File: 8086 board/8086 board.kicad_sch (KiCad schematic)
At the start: 9 parts, among them U1 P8086-2, U23 74HC14, U27 74HC02, U8 74AC00

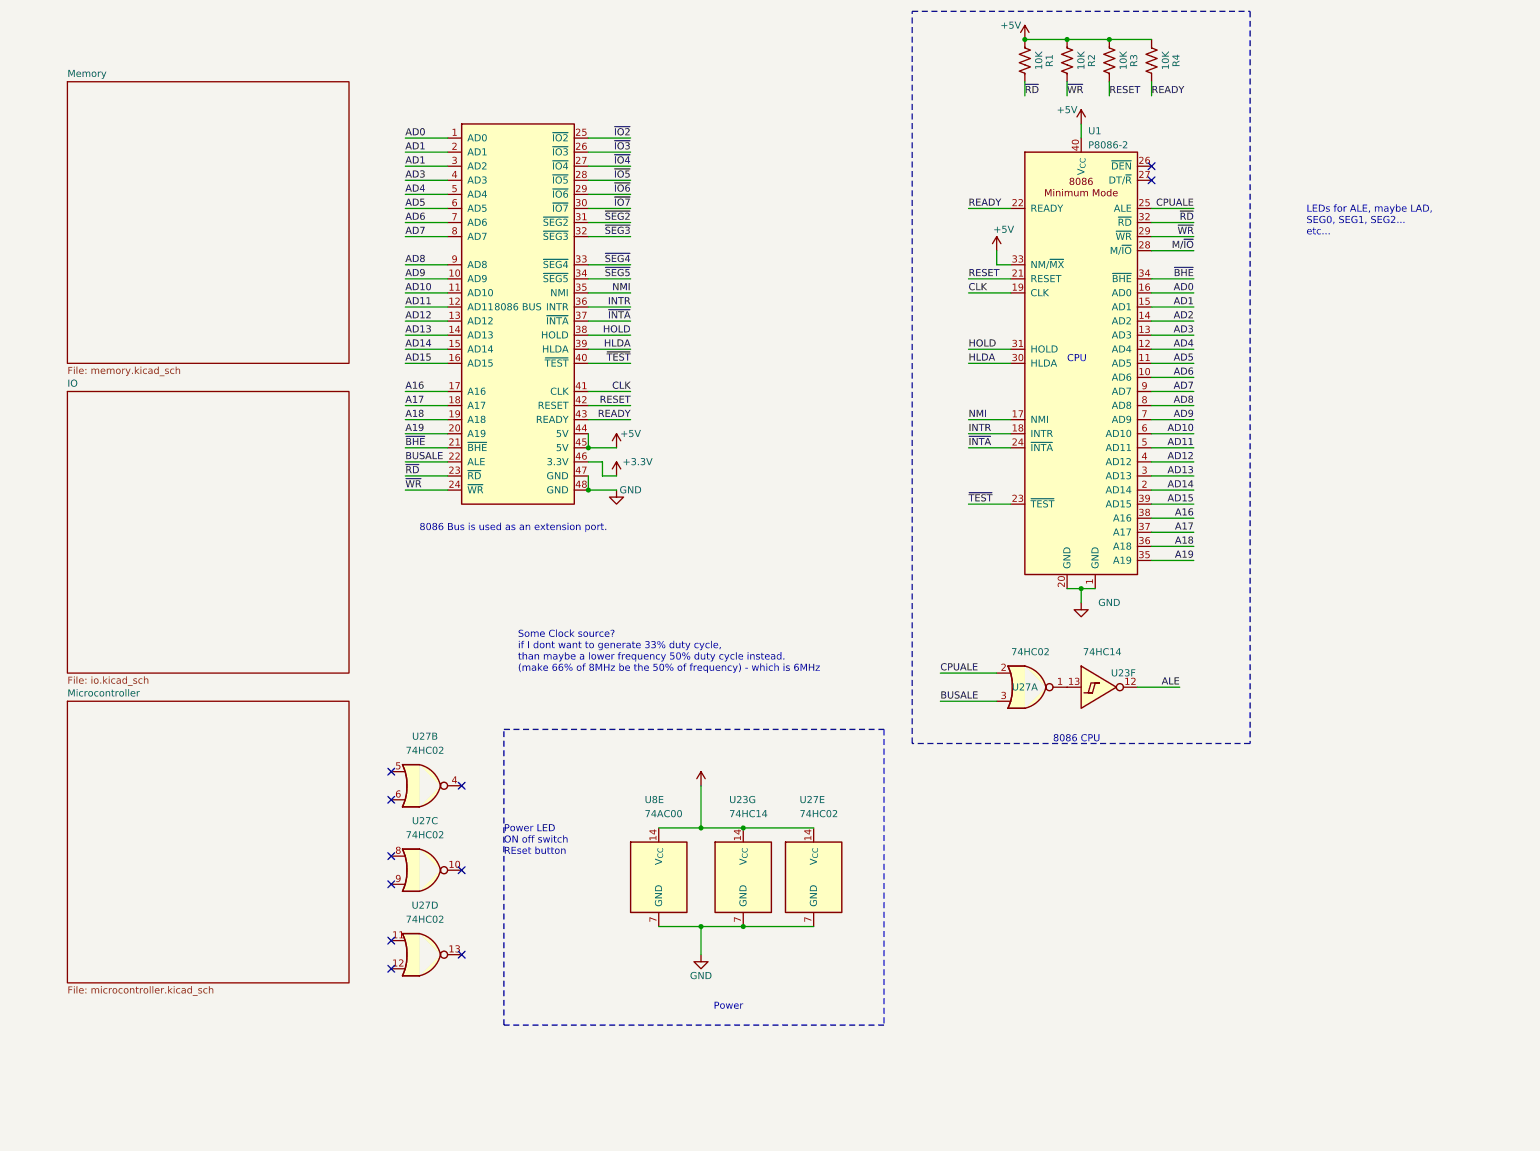
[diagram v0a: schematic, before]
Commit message: better schematic. initial pcb layout
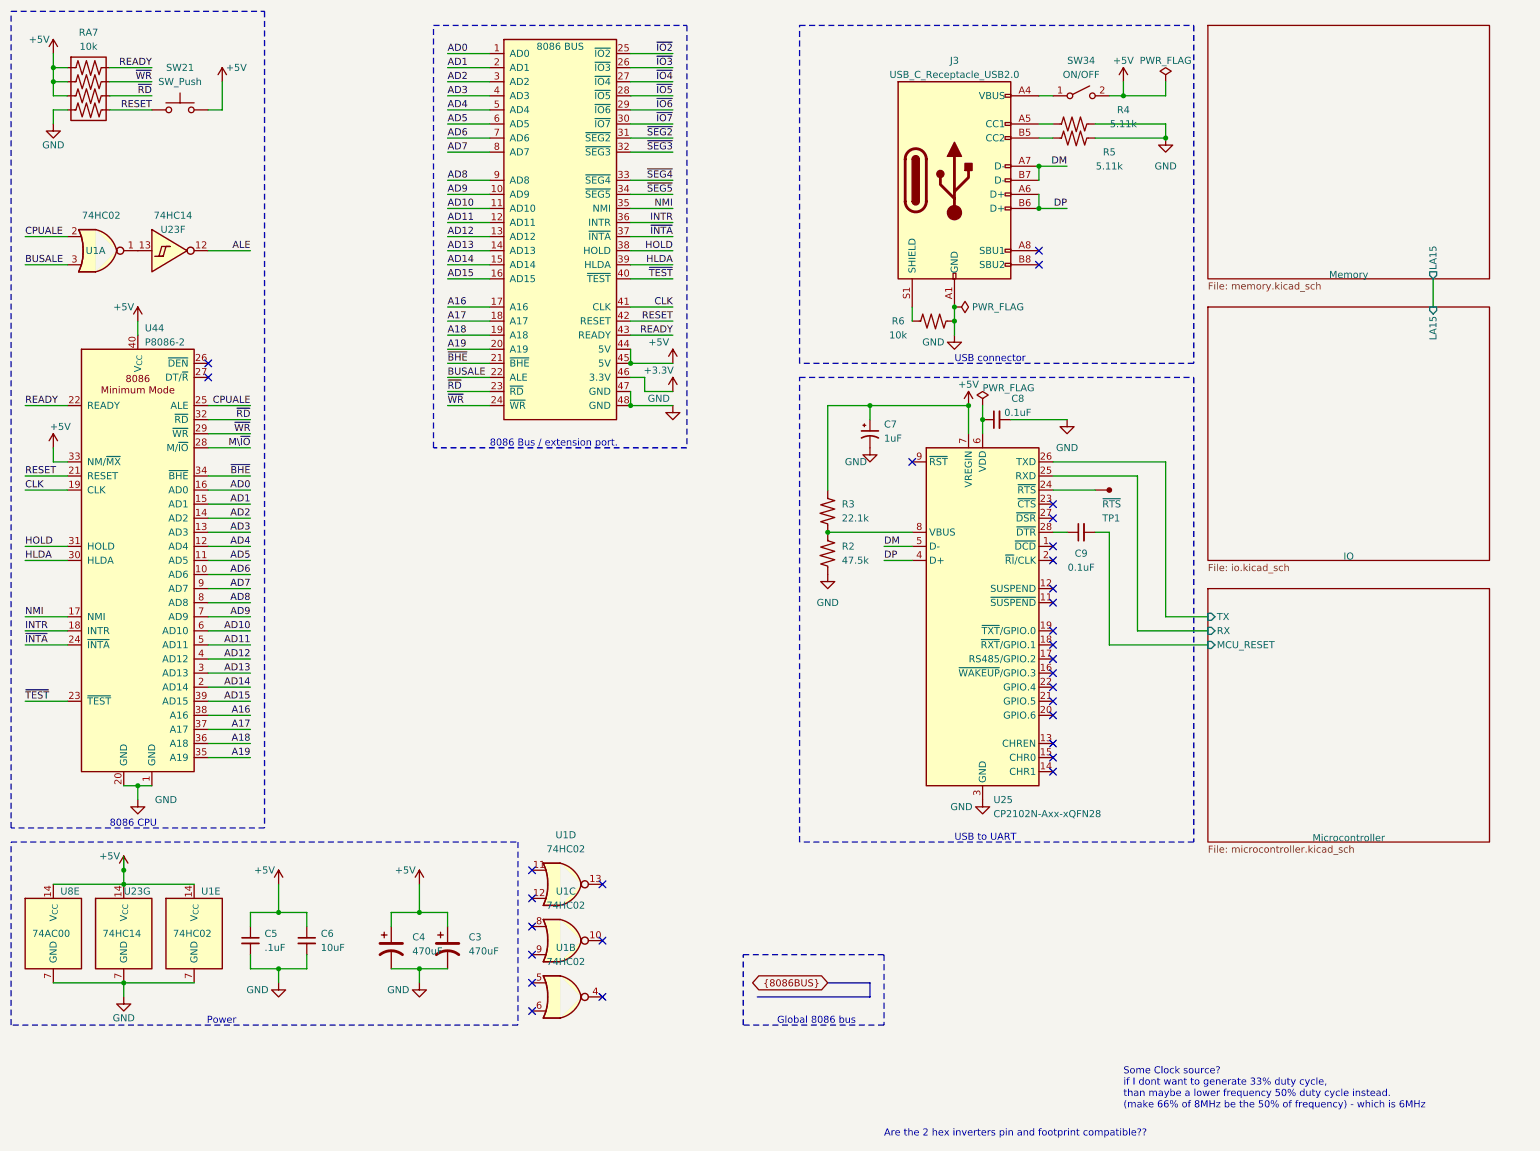
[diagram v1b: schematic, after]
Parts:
- removed R1, R2, R3, R4: 10K, Resistor_SMD:R_0603_1608Metric_Pad0.98x0.95mm_HandSolder, symbol Device:R_US
- added C3, C4: 470uF, symbol Device:C_Polarized_US
- added C5: .1uF, symbol Device:C_Small
- added C6: 10uF, symbol Device:C_Small
- added C7: 1uF, symbol Device:C_Polarized_Small_US
- added C8, C9: 0.1uF, symbol Device:C_Small
- added J3: USB_C_Receptacle_USB2.0, symbol Connector:USB_C_Receptacle_USB2.0
- added R2: 47.5k, symbol 8086PC:R
- added R3: 22.1k, symbol 8086PC:R
- added R4, R5: 5.11k, symbol 8086PC:R
- added R6: 10k, symbol 8086PC:R
- added RA7: 10k, Resistor_SMD:R_Array_Concave_4x0603, symbol 8086PC:R_Array_4
- added SW21: SW_Push, Button_Switch_SMD:SW_Push_1P1T_NO_6x6mm_H9.5mm, symbol Switch:SW_Push
- added SW34: ON/OFF, symbol Switch:SW_SPST
- added TP1: ~{RTS}, symbol 8086PC:TestPoint
- added U25: CP2102N-Axx-xQFN28, Package_DFN_QFN:QFN-28-1EP_5x5mm_P0.5mm_EP3.35x3.35mm, symbol Interface_USB:CP2102N-Axx-xQFN28
- renumbered U27 to U1, U1 to U44
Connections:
- net +5V: now also C3.1, C4.1, C5.1, C6.1, C7.1, R3.1, RA7.1, RA7.2, RA7.3, SW21.1, SW34.2 (B), U25.7 (VREGIN)
- net AD1: no longer BUS1.3 (AD2)
- net AD2: now also BUS1.3 (AD2)
- net GND: now also C3.2, C4.2, C5.2, C6.2, C7.2, C8.2, J3.A1 (GND), J3.A12 (GND), J3.B1 (GND), J3.B12 (GND), R2.2, R4.2, R5.2, R6.2, RA7.4, U25.29 (GND), U25.3 (GND)
- net READY: now also RA7.8
- net RESET: now also RA7.5, SW21.2
- net ~{RD}: now also RA7.6
- net ~{WR}: now also RA7.7
- net M/~{IO} renamed M\~{IO}
- new net: J3.B5 (CC2), R5.1
- new net: TP1.1, U25.24 (~{RTS})
- new net: C9.1, U25.28 (~{DTR})
- new net: C8.1, U25.6 (VDD)
- new net: R2.1, R3.2, U25.8 (VBUS)
- new net: J3.A4 (VBUS), J3.A9 (VBUS), J3.B4 (VBUS), J3.B9 (VBUS), SW34.1 (A)
- new net: J3.S1 (SHIELD), R6.1
- new net: J3.A5 (CC1), R4.1
- new net DM: J3.A7 (D-), J3.B7 (D-), U25.5 (D-)
- new net DP: J3.A6 (D+), J3.B6 (D+), U25.4 (D+)
- new net Microcontroller/MCU_RESET: C9.2
- new net Microcontroller/RX: U25.25 (RXD)
- new net Microcontroller/TX: U25.26 (TXD)
- no-connect marks 11 -> 30
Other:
- sheet IO ports: added LA15; removed none
- sheet Memory ports: added LA15; removed none
- sheet Microcontroller ports: added MCU_RESET, RX, TX; removed none
- note added: "8086 Bus / extension port."
- note added: "Are the 2 hex inverters pin and footprint compatible??"
- note added: "Global 8086 bus"
- note added: "USB connector"
- note added: "USB to UART"
- note removed: "8086 Bus is used as an extension port."
- note removed: "CPU"
- note removed: "LEDs for ALE, maybe LAD, SEG0, SEG1, SEG2... etc..."
- note removed: "Power LED ON off switch REset button"
- moved on the sheet: U1A, U1B, U1C, U1D, U1E, U23F, U23G, U44, U8E

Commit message: Schematic finished! (some footprint assignments are still needed)
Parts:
- removed C3: 470uF, symbol Device:C_Polarized_US
- removed C5: .1uF, symbol Device:C_Small
- removed C6: 10uF, symbol Device:C_Small
- removed C7: 1uF, symbol Device:C_Polarized_Small_US
- removed unit 3 of U1
- removed unit 2 of U1
- added C? (x36): 1uF, Capacitor_SMD:C_0603_1608Metric_Pad1.08x0.95mm_HandSolder, symbol Device:C_Small
- added C? (x2): 10uF, Capacitor_SMD:C_0603_1608Metric_Pad1.08x0.95mm_HandSolder, symbol Device:C_Polarized_US
- added U?: 74HC02, Package_SO:SOIC-14_3.9x8.7mm_P1.27mm, symbol 8086PC:74HC02
- added U?: AMS1117-3.3, Package_TO_SOT_SMD:SOT-223-3_TabPin2, symbol Regulator_Linear:AMS1117-3.3
- BUS1: footprint Package_DIP:SMDIP-64_W15.24mm -> Connector_PinHeader_2.54mm:PinHeader_2x24_P2.54mm_Vertical
- C4: renamed from C8; value 0.1uF -> 1uF; footprint (none) -> Capacitor_SMD:C_0603_1608Metric_Pad1.08x0.95mm_HandSolder
- C5: renamed from C9; footprint (none) -> Capacitor_SMD:C_0603_1608Metric_Pad1.08x0.95mm_HandSolder
- R1: renamed from R4; footprint (none) -> Resistor_SMD:R_0603_1608Metric_Pad0.98x0.95mm_HandSolder
- R2: renamed from R5; footprint (none) -> Resistor_SMD:R_0603_1608Metric_Pad0.98x0.95mm_HandSolder
- R3: renamed from R6; footprint (none) -> Resistor_SMD:R_0603_1608Metric_Pad0.98x0.95mm_HandSolder
- R4: renamed from R3; footprint (none) -> Resistor_SMD:R_0603_1608Metric_Pad0.98x0.95mm_HandSolder
- R5: renamed from R2; footprint (none) -> Resistor_SMD:R_0603_1608Metric_Pad0.98x0.95mm_HandSolder
- SW34: value ON/OFF -> POWER
- SW?: renamed from SW21; value SW_Push -> RESET; footprint Button_Switch_SMD:SW_Push_1P1T_NO_6x6mm_H9.5mm -> 8086PC:SW_Push_1P1T_NO_6x6mm_H9.5mm; symbol Switch:SW_Push -> 8086PC:SW_Push
- TP1: footprint (none) -> TestPoint:TestPoint_Pad_1.5x1.5mm
- renumbered C4 to C?, J3 to J1, RA7 to RA1, U44 to U1, U8 to U2, U23 to U3, U1 to U4, U25 to U?
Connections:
- net +3.3V: now also BUS1.44 (3.3V), C?.1, U?.2 (VO); no longer BUS1.46 (3.3V)
- net +5V: now also BUS1.40 (5V), BUS1.42 (5V), C?.1, C?.1, C?.1, C?.1, C?.1, C?.1, C?.1, C?.1, C?.1, C?.1, C?.1, C?.1, C?.1, C?.1, C?.1, C?.1, C?.1, C?.1, C?.1, C?.1, C?.1, C?.1, C?.1, C?.1, C?.1, C?.1, C?.1, C?.1, C?.1, C?.1, C?.1, C?.1, C?.1, C?.1, C?.1, C?.1, C?.1, U?.14 (V_{CC}), U?.3 (VI); no longer BUS1.44 (5V), BUS1.45 (5V)
- net A16: now also BUS1.33 (A16); no longer BUS1.17 (A16)
- net A17: now also BUS1.35 (A17); no longer BUS1.18 (A17)
- net A18: now also BUS1.37 (A18); no longer BUS1.19 (A18)
- net A19: now also BUS1.39 (A19); no longer BUS1.20 (A19)
- net AD1: now also BUS1.3 (AD1); no longer BUS1.2 (AD1)
- net AD10: now also BUS1.21 (AD10); no longer BUS1.11 (AD10)
- net AD11: now also BUS1.23 (AD11); no longer BUS1.12 (AD11)
- net AD12: now also BUS1.25 (AD12); no longer BUS1.13 (AD12)
- net AD13: now also BUS1.27 (AD13); no longer BUS1.14 (AD13)
- net AD14: now also BUS1.29 (AD14); no longer BUS1.15 (AD14)
- net AD15: now also BUS1.31 (AD15); no longer BUS1.16 (AD15)
- net AD2: now also BUS1.5 (AD2); no longer BUS1.3 (AD2)
- net AD3: now also BUS1.7 (AD3); no longer BUS1.4 (AD3)
- net AD4: now also BUS1.9 (AD4); no longer BUS1.5 (AD4)
- net AD5: now also BUS1.11 (AD5); no longer BUS1.6 (AD5)
- net AD6: now also BUS1.13 (AD6); no longer BUS1.7 (AD6)
- net AD7: now also BUS1.15 (AD7); no longer BUS1.8 (AD7)
- net AD8: now also BUS1.17 (AD8); no longer BUS1.9 (AD8)
- net AD9: now also BUS1.19 (AD9); no longer BUS1.10 (AD9)
- net BUSALE: now also BUS1.43 (ALE); no longer BUS1.22 (ALE)
- net CLK: now also BUS1.34 (CLK); no longer BUS1.41 (CLK)
- net GND: now also BUS1.46 (GND), C?.2, C?.2, C?.2, C?.2, C?.2, C?.2, C?.2, C?.2, C?.2, C?.2, C?.2, C?.2, C?.2, C?.2, C?.2, C?.2, C?.2, C?.2, C?.2, C?.2, C?.2, C?.2, C?.2, C?.2, C?.2, C?.2, C?.2, C?.2, C?.2, C?.2, C?.2, C?.2, C?.2, C?.2, C?.2, C?.2, C?.2, C?.2, U?.1 (GND), U?.7 (GND); no longer BUS1.47 (GND)
- net HLDA: now also BUS1.30 (HLDA); no longer BUS1.39 (HLDA)
- net HOLD: now also BUS1.28 (HOLD); no longer BUS1.38 (HOLD)
- net INTR: now also BUS1.24 (INTR); no longer BUS1.36 (INTR)
- net NMI: now also BUS1.22 (NMI); no longer BUS1.35 (NMI)
- net READY: now also BUS1.38 (READY); no longer BUS1.43 (READY)
- net RESET: now also BUS1.36 (RESET); no longer BUS1.42 (RESET)
- net ~{BHE}: now also BUS1.41 (~{BHE}); no longer BUS1.21 (~{BHE})
- net ~{INTA}: now also BUS1.26 (~{INTA}); no longer BUS1.37 (~{INTA})
- net ~{IO2}: now also BUS1.2 (~{IO2}); no longer BUS1.25 (~{IO2})
- net ~{IO3}: now also BUS1.4 (~{IO3}); no longer BUS1.26 (~{IO3})
- net ~{IO4}: now also BUS1.6 (~{IO4}); no longer BUS1.27 (~{IO4})
- net ~{IO5}: now also BUS1.8 (~{IO5}); no longer BUS1.28 (~{IO5})
- net ~{IO6}: now also BUS1.10 (~{IO6}); no longer BUS1.29 (~{IO6})
- net ~{IO7}: now also BUS1.12 (~{IO7}); no longer BUS1.30 (~{IO7})
- net ~{RD}: now also BUS1.45 (~{RD}); no longer BUS1.23 (~{RD})
- net ~{SEG2}: now also BUS1.14 (~{SEG2}); no longer BUS1.31 (~{SEG2})
- net ~{SEG3}: now also BUS1.16 (~{SEG3}); no longer BUS1.32 (~{SEG3})
- net ~{SEG4}: now also BUS1.18 (~{SEG4}); no longer BUS1.33 (~{SEG4})
- net ~{SEG5}: now also BUS1.20 (~{SEG5}); no longer BUS1.34 (~{SEG5})
- net ~{TEST}: now also BUS1.32 (~{TEST}); no longer BUS1.40 (~{TEST})
- net ~{WR}: now also BUS1.47 (~{WR}); no longer BUS1.24 (~{WR})
- no-connect marks 30 -> 24
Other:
- note added: "8086 Bus / extension port"
- note added: "Decoupling capacitors"
- note added: "Unused"
- note removed: "8086 Bus / extension port."
- note removed: "Are the 2 hex inverters pin and footprint compatible??"
- note removed: "Some Clock source? if I dont want to generate 33% duty cycle, than maybe a lower frequency 50% duty cycle instead. (make 66% of 8MHz be the 50% of frequency) - which is 6MHz"
- moved on the sheet: C4, C?, RA1, U1, U2E, U3F, U3G, U4A, U4D, U4E
